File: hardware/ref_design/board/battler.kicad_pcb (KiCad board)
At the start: 2 copper layers, 70.4 x 151.2 mm, 122 parts, among them J1 TYPE-C-31-M-12, J2 S2B-PH-SM4-TB, J3 FH12-50S-0.5SH(55), J4 SPEAKER, J5 SWD, J6 UART, Q1 2N7002, Q2 AO3401A, Q3 2N7002, SW1 P1 UP, SW10 P2 DOWN, SW11 P2 LEFT, SW12 P2 RIGHT, SW13 P2 A, SW14 P2 B, SW15 P2 X, SW16 P2 Y, SW18 BOOTSEL, SW19 RESET, SW2 P1 DOWN, SW3 P1 LEFT, SW4 P1 RIGHT, SW5 P1 A, SW6 P1 B, SW7 P1 X, SW8 P1 Y / PWR, SW9 P2 UP, U1 SRV05-4, U2 TP4056-42-ESOP8, U3 ME6211C33M5G, U4 RP2354B, U6 AP3156FVG-7, U7 FM8002A, X1 12MHz

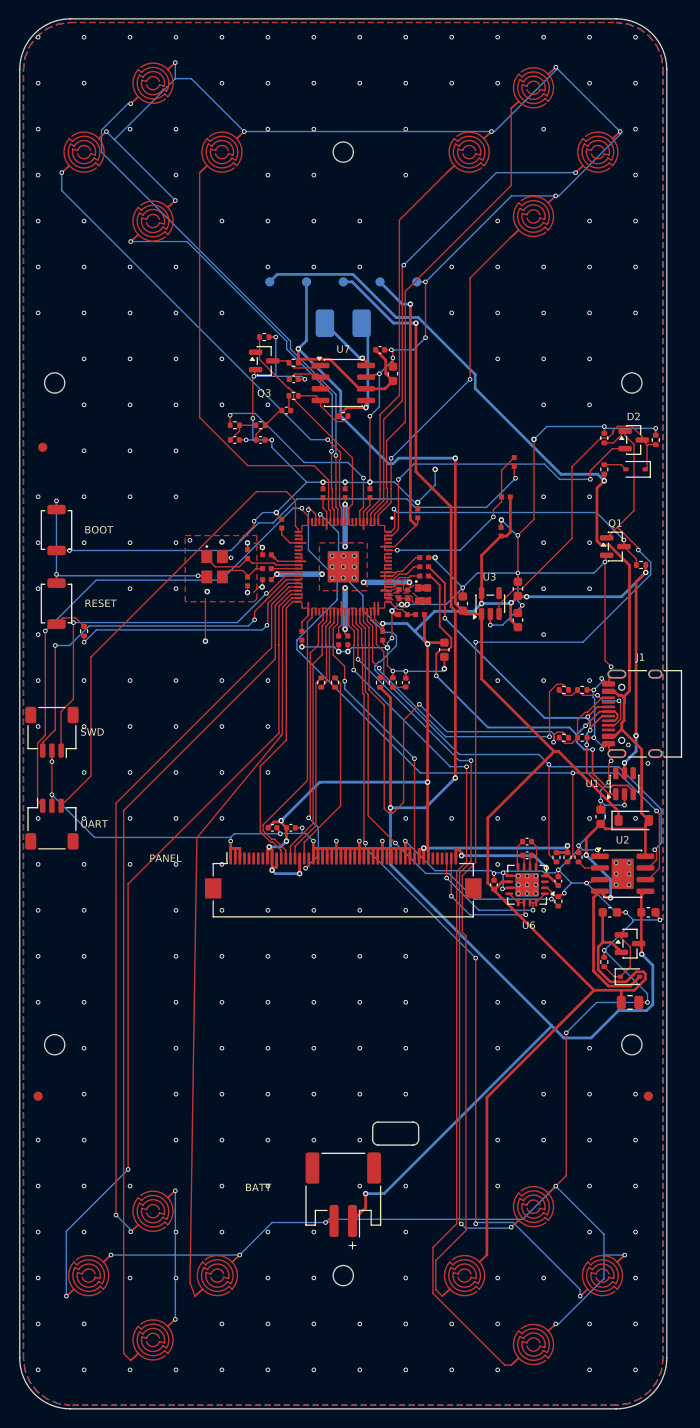
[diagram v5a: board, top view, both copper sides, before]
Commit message: Reference design: audit round 2 fixes (VBUS bleeder, window, fit check)
- R15 back to 100k and a 10k VBUS bleeder (R38) instead: the 10k R15 cut the
  Y contact's pill-resistance margin for Q1 about five times. The bleeder
  needs about 140 uA of D5 leakage before CE reaches 1.0 V; 0.5 mA on USB.
  R38 sits beside R14 (next to C1 it blocked seat 1's A route).
- Lid window margin 0.5 -> 0.8 mm: covers the panel's +-0.4 float in its
  frame and its +-0.3 active-area tolerance. Frame wall and depth named.
- check_fit.py knows the lid's panel frame: parts under its band are held
  to its lower limit (3.6 mm).
- route.py: the final cleanup also drops a pour's via that joins nothing
  (a stitching via left in a pocket the pours never reached).

Checks: netlist PASS (123 parts), ERC 0, DRC 0 errors / 0 unconnected /
0 parity (2 cosmetic silk warnings), fit PASS on 92 parts.

Co-Authored-By: Claude Opus 5.5 <noreply@anthropic.com>
Claude-Session: https://claude.ai/code/session_01KGgEu3CbFtCsvHRQgAFiCN
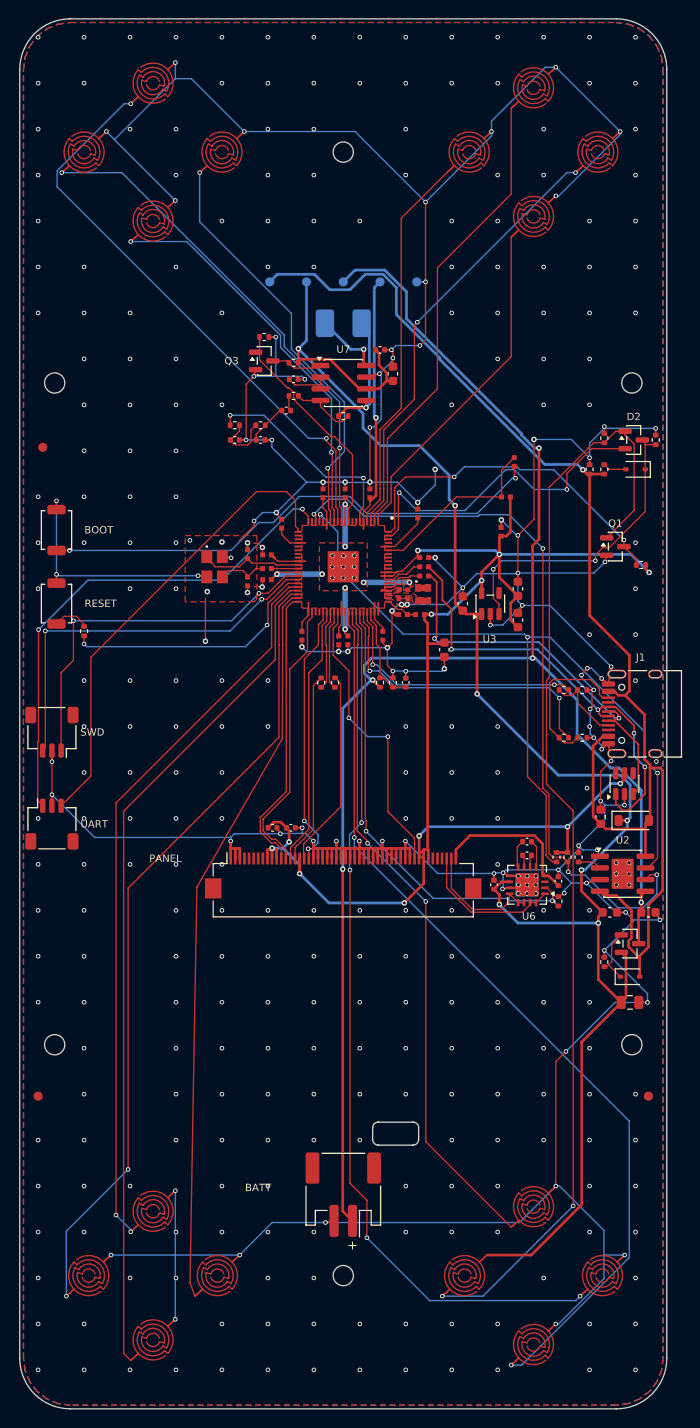
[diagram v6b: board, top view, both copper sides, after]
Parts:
- added R38: 10k, Resistor_SMD:R_0402_1005Metric, F.Cu at (126.8, 73.4)
- R15: value 10k -> 100k
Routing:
- net CC2_SENSE: track 56.1 -> 33.4 mm
- net VBUS: track 127.7 -> 146.8 mm, vias 3 -> 1
- net CHG_STAT_N: track 79.0 -> 90.8 mm
- net P1_A: track 88.2 -> 97.0 mm
- net VSYS: track 191.4 -> 183.1 mm, vias 2 -> 7
- net +3V3: track 227.8 -> 219.9 mm, vias 17 -> 13
- net /USB_Charger/CC2: track 8.81 -> 16.6 mm
- net CC1_SENSE: track 36.0 -> 28.4 mm
- net P1_B: track 94.9 -> 101.7 mm
- net USB_DM: track 49.4 -> 43.2 mm, vias 3 -> 2
- net USB_DP: track 42.3 -> 48.3 mm
- net P2_B: track 58.7 -> 64.1 mm
- net PWR_BTN_N: track 33.0 -> 38.2 mm
- net GND: track 666.4 -> 671.5 mm, vias 357 -> 363
- net P1_X: track 80.1 -> 75.3 mm, vias 4 -> 2
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
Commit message: Reference design: audit round 3 fixes (unplug hand-over, panel stack)
- R38 (VBUS bleeder) 10k -> 1k. At an unplug C1 held VBUS up, and Q2's gate,
  fed from VBUS through D6, could only fall as fast as VBUS: the body diode
  carried the system for tens of ms at the cell less 0.5 V. Now Q2 conducts
  about 3 ms after an unplug, fully on after about 8 ms. 5 mA on USB. The
  design review's "microseconds" description of the hand-over was wrong and
  is rewritten; the bring-up unplug test says what to expect.
- Panel counted as 2.45 mm (the drawing's side view says 2.35 +-0.1) and the
  0.15 mm tape is in the stack: the glass limit drops to 2.1 mm (J3's 2.0 mm
  still clears). Window margin 1.0 mm (float, tolerance and print error).
  The lid's FPC notch widened: the drawing doesn't dimension the neck, so
  fpc_neck is marked ESTIMATE.

Checks: netlist PASS (123 parts), ERC 0, DRC 0 errors / 0 unconnected /
0 parity (2 cosmetic silk warnings), fit PASS on 92 parts.

Co-Authored-By: Claude Opus 5.5 <noreply@anthropic.com>
Claude-Session: https://claude.ai/code/session_01KGgEu3CbFtCsvHRQgAFiCN
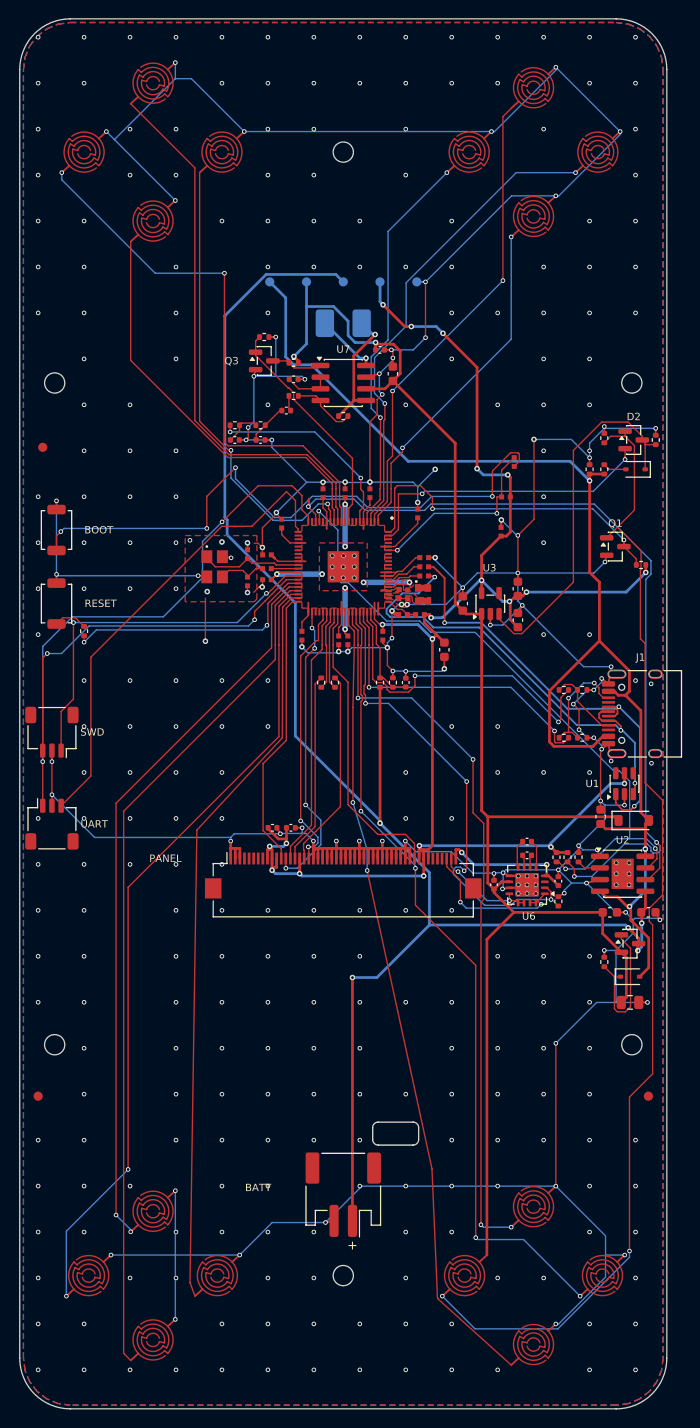
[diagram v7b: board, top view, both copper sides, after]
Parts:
- R38: value 10k -> 1k
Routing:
- net CHG_STAT_N: track 90.8 -> 73.9 mm
- net CHG_DONE_N: track 81.4 -> 95.5 mm, vias 4 -> 3
- net P1_B: track 101.7 -> 87.9 mm
- net VSYS: track 183.1 -> 171.5 mm, vias 7 -> 2
- net /Debug/BOOTSEL: track 56.1 -> 67.2 mm, vias 2 -> 4
- net /USB_Charger/LS_GATE: track 6.21 -> 16.1 mm
- net P1_A: track 97.0 -> 88.8 mm
- net USB_DM: track 43.2 -> 51.2 mm, vias 2 -> 3
- net CC1_SENSE: track 28.4 -> 35.9 mm
- net /Power/PWR_EN: track 33.7 -> 40.4 mm, vias 2 -> 0
- net VBUS: track 146.8 -> 141.2 mm, vias 1 -> 3
- net P1_X: track 75.3 -> 80.7 mm, vias 2 -> 4
- net P2_A: track 55.5 -> 60.9 mm
- net P2_Y: track 46.5 -> 51.3 mm
- net /USB_Charger/CC2: track 16.6 -> 12.3 mm, vias 0 -> 2
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
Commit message: Reference design: audio filter 4.7 nF, PWM at 8 bits (586 kHz)
C37/C38 10 nF -> 4.7 nF (C1538, a JLC basic part; C37/C38 were the only
users of the 10 nF part, so the BOM stays at 37 part numbers). With the PWM
at 8 bits (150 MHz / 256 = 586 kHz) the audio band is -3 dB at about 14 kHz
instead of 6.6 kHz, and the carrier comes out 49 dB down instead of 38.
Firmware must run 8 bits: 10-bit PWM (146 kHz) would only be 26 dB down.
Pin map, bring-up, design review, PLAN and the schematic note say so.
(3.9 nF, which would give 17 kHz, is only an extended part at JLC.)

Checks: netlist PASS, ERC 0, DRC 0 errors / 0 unconnected / 0 parity,
fit PASS.

Co-Authored-By: Claude Opus 5.5 <noreply@anthropic.com>
Claude-Session: https://claude.ai/code/session_01KGgEu3CbFtCsvHRQgAFiCN
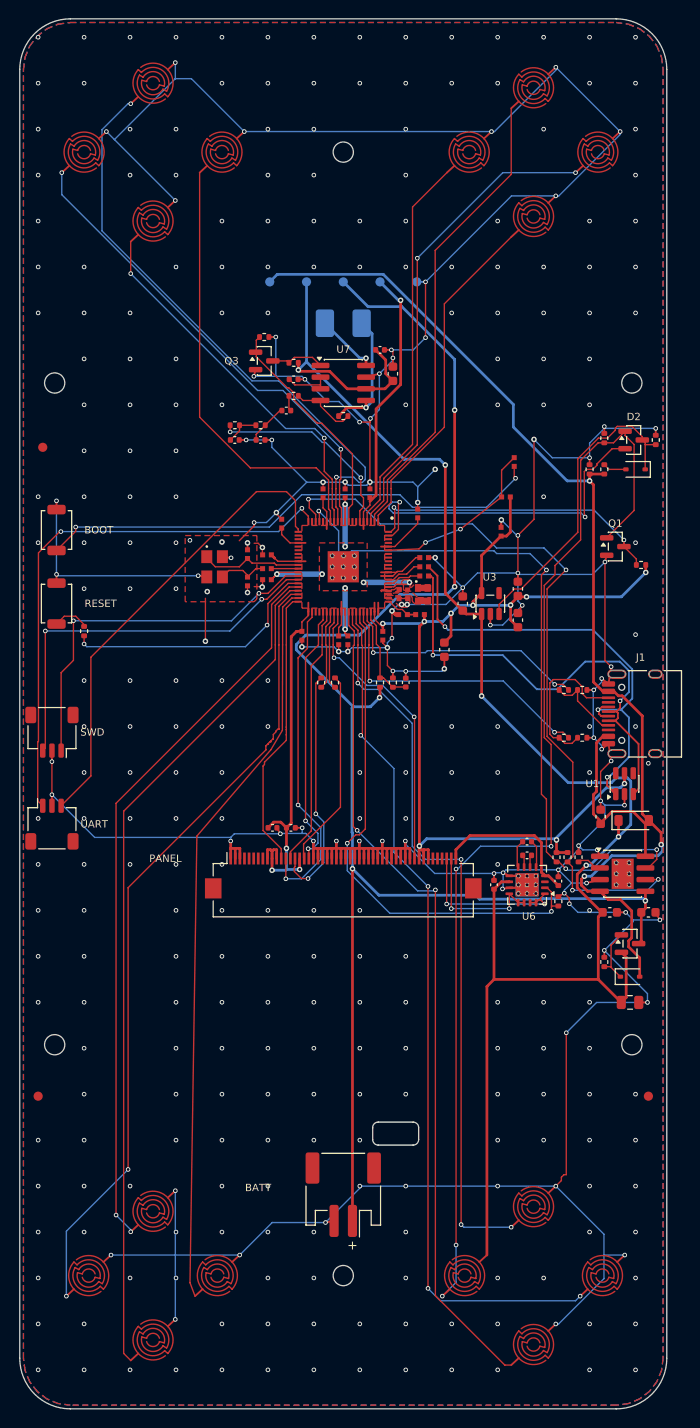
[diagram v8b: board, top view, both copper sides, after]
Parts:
- C37, C38: value 10n -> 4.7n
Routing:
- net VSYS: track 171.5 -> 185.8 mm, vias 2 -> 5
- net CHG_DONE_N: track 95.5 -> 82.8 mm, vias 3 -> 4
- net /Debug/BOOTSEL: track 67.2 -> 56.0 mm, vias 4 -> 2
- net /USB_Charger/LS_GATE: track 16.1 -> 6.17 mm
- net CC1_SENSE: track 35.9 -> 27.8 mm
- net P2_A: track 60.9 -> 53.4 mm
- net P1_A: track 88.8 -> 95.4 mm
- net PWR_HOLD: track 32.6 -> 38.6 mm
- net BL_SDI: track 51.7 -> 57.4 mm, vias 4 -> 2
- net /Power/PWR_EN: track 40.4 -> 34.8 mm
- net /Display/LCD_SCK: track 20.8 -> 26.4 mm, vias 0 -> 2
- net CHG_STAT_N: track 73.9 -> 79.2 mm, vias 3 -> 4
- net VBAT: track 174.2 -> 169.3 mm
- net /USB_Charger/CC2: track 12.3 -> 17.0 mm, vias 2 -> 0
- net P2_B: track 60.9 -> 65.5 mm, vias 0 -> 2
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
